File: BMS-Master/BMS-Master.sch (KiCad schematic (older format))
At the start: 14 parts

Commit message: schematics updates
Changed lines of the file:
@@
 $EndSheet
-Wire Wire Line
-	5100 3100 5550 3100
 Wire Wire Line
 	5100 3700 6300 3700
@@
 Wire Wire Line
 	8950 3000 9550 3000
-$Comp
-L power:GND #PWR?
-U 1 1 5AC38521
-P 5550 3200
-F 0 "#PWR?" H 5550 2950 50  0001 C CNN
-F 1 "GND" H 5555 3027 50  0000 C CNN
-F 2 "" H 5550 3200 50  0001 C CNN
-F 3 "" H 5550 3200 50  0001 C CNN
-	1    5550 3200
-	1    0    0    -1
-$EndComp
-Wire Wire Line
-	5550 3200 5550 3100
-Connection ~ 5550 3100
-Wire Wire Line
-	5550 3100 6300 3100
+Wire Wire Line
+	5100 3100 6300 3100
 $EndSCHEMATC

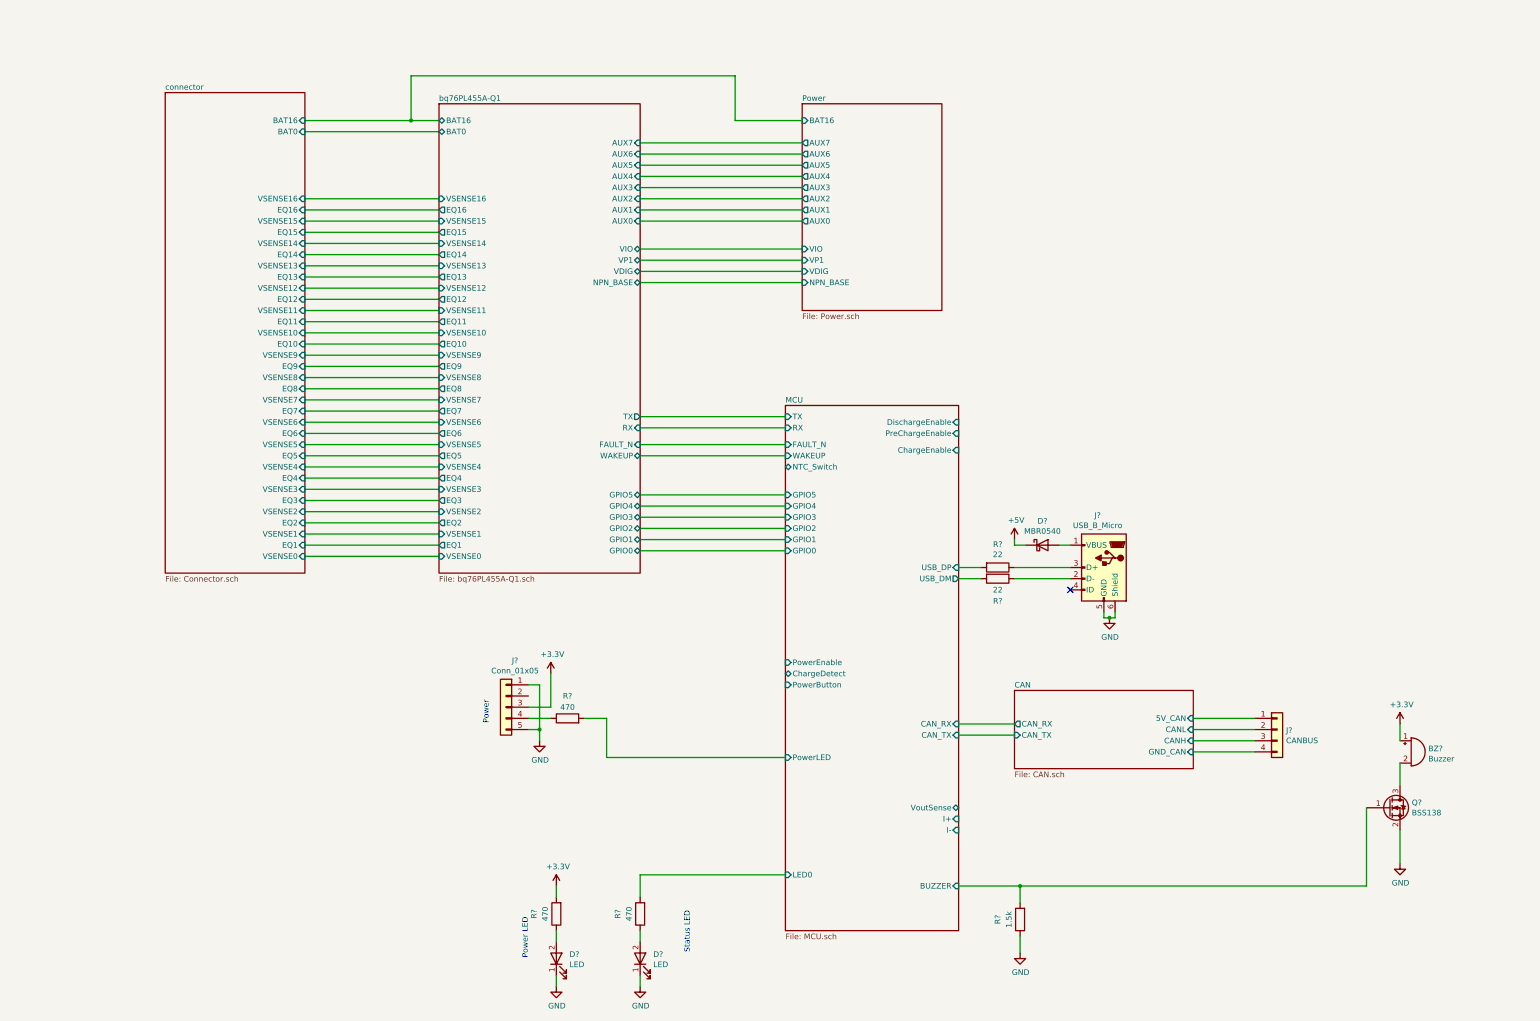
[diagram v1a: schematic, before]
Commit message: schematic update
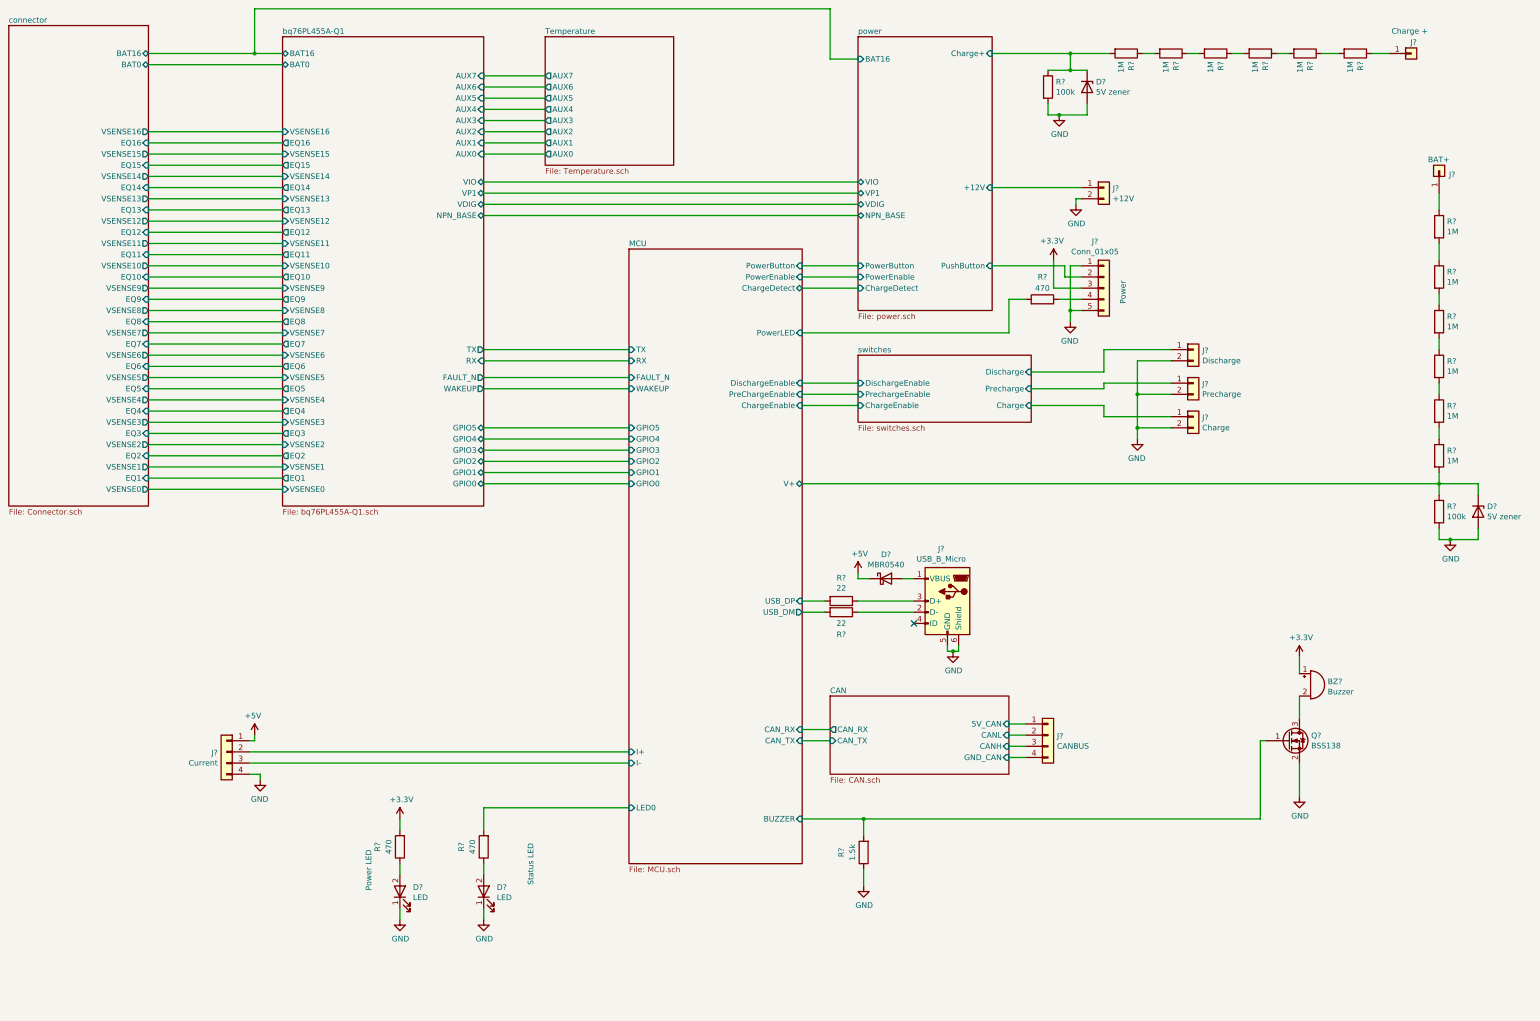
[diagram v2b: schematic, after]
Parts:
- added D? (x2): 5V zener, symbol Device:D_Zener
- added J?: Charge +, symbol Connector_Generic:Conn_01x01
- added J?: Current, symbol Connector_Generic:Conn_01x04
- added J?: +12V, symbol Connector_Generic:Conn_01x02
- added J?: Discharge, symbol Connector_Generic:Conn_01x02
- added J?: Precharge, symbol Connector_Generic:Conn_01x02
- added J?: Charge, symbol Connector_Generic:Conn_01x02
- added J?: BAT+, symbol Connector_Generic:Conn_01x01
- added R? (x12): 1M, Resistors_SMD:R_1206, symbol Device:R
- added R? (x2): 100k, Resistors_SMD:R_1206, symbol Device:R
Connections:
- net +5V: now also J?.1 (Pin_1)
- net GND: now also D?.2 (A), D?.2 (A), J?.2 (Pin_2), J?.2 (Pin_2), J?.2 (Pin_2), J?.2 (Pin_2), J?.4 (Pin_4), R?.2, R?.2
- net MCU/I+: now also J?.2 (Pin_2)
- net MCU/I-: now also J?.3 (Pin_3)
- net power/PushButton: now reaches J?.2 (Pin_2)
- new net: R?.1, R?.2 (x10)
- new net: J?.1 (Pin_1), R?.1 (x2)
- new net MCU/V+: D?.1 (K), R?.1, R?.2
- new net power/+12V: J?.1 (Pin_1)
- new net power/Charge+: D?.1 (K), R?.1, R?.2
- new net switches/Charge: J?.1 (Pin_1)
- new net switches/Discharge: J?.1 (Pin_1)
- new net switches/Precharge: J?.1 (Pin_1)
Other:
- moved on the sheet: BZ?, D?, J?, Q?, R?

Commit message: update
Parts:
- removed D? (x2): 5V zener, symbol Device:D_Zener
- removed J?: Charge +, symbol Connector_Generic:Conn_01x01
- removed J?: BAT+, symbol Connector_Generic:Conn_01x01
- removed R? (x12): 1M, Resistors_SMD:R_1206, symbol Device:R
- removed R? (x2): 100k, Resistors_SMD:R_1206, symbol Device:R
- added F?: Fuse, symbol Device:Fuse
- added J?: Charge +, symbol Connector_Generic:Conn_01x01
- added J?: BAT+, symbol Connector_Generic:Conn_01x01
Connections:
- net power/+12V: now also F?.2; no longer J?.1 (Pin_1)
- net power/Charge+: now also J?.1 (Pin_1)
- new net: F?.1, J?.1 (Pin_1)
- new net power/Bat+: J?.1 (Pin_1)
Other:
- moved on the sheet: J?
